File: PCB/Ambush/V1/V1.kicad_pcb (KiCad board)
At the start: 2 copper layers, 46.5 x 54.6 mm, 7 parts, among them J1 Pines Motores, J2 Screw_Terminal_01x02, SW1 SW ON/OFF, U2 ESP32-Devkit-V1

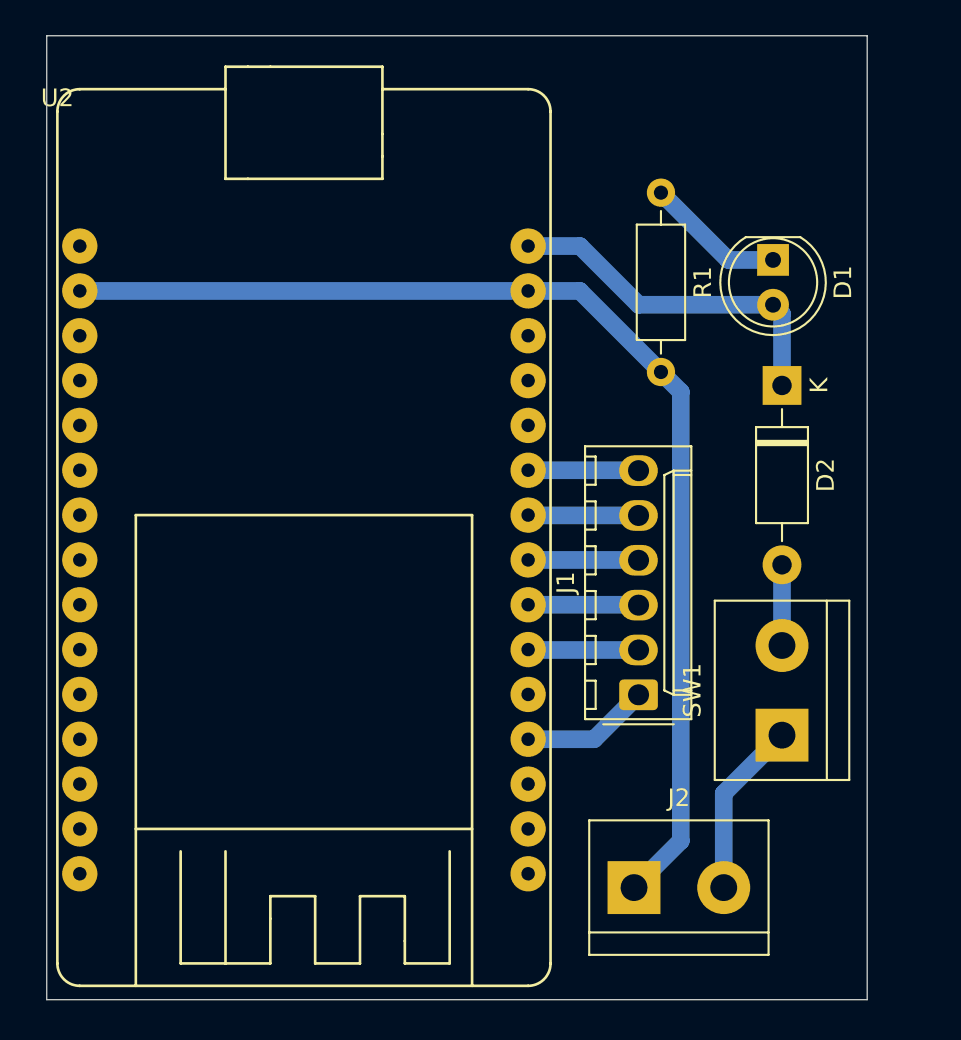
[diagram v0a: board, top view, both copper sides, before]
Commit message: PCB Con testpoint
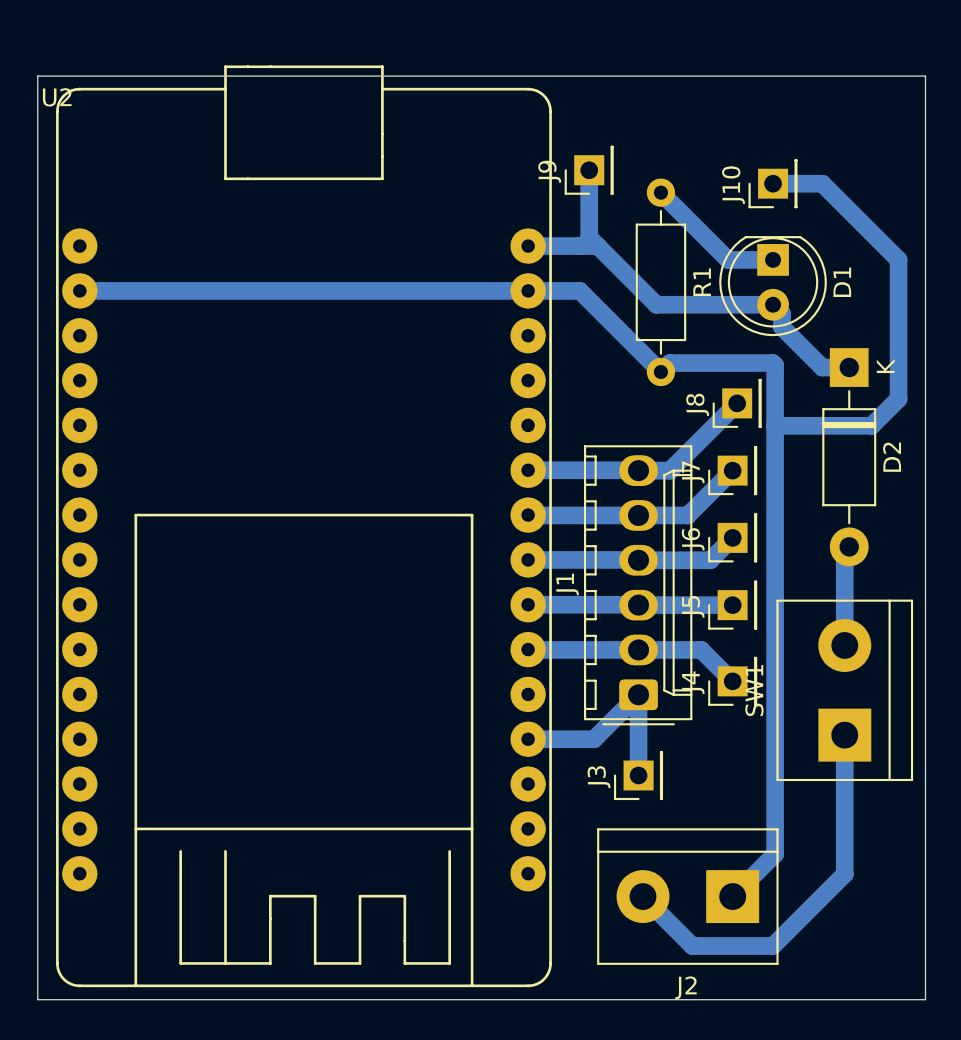
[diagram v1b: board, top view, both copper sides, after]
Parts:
- added J10: Conn_01x01_Pin, Connector_PinHeader_2.54mm:PinHeader_1x01_P2.54mm_Vertical, F.Cu at (141.2, 51.1)
- added J3: Conn_01x01_Pin, Connector_PinHeader_2.54mm:PinHeader_1x01_P2.54mm_Vertical, F.Cu at (133.6, 84.6)
- added J4: Conn_01x01_Pin, Connector_PinHeader_2.54mm:PinHeader_1x01_P2.54mm_Vertical, F.Cu at (138.9, 79.2)
- added J5: Conn_01x01_Pin, Connector_PinHeader_2.54mm:PinHeader_1x01_P2.54mm_Vertical, F.Cu at (138.9, 74.9)
- added J6: Conn_01x01_Pin, Connector_PinHeader_2.54mm:PinHeader_1x01_P2.54mm_Vertical, F.Cu at (138.9, 71.1)
- added J7: Conn_01x01_Pin, Connector_PinHeader_2.54mm:PinHeader_1x01_P2.54mm_Vertical, F.Cu at (138.9, 67.3)
- added J8: Conn_01x01_Pin, Connector_PinHeader_2.54mm:PinHeader_1x01_P2.54mm_Vertical, F.Cu at (139.2, 63.5)
- added J9: Conn_01x01_Pin, Connector_PinHeader_2.54mm:PinHeader_1x01_P2.54mm_Vertical, F.Cu at (130.8, 50.3)
- moved J2 5.61 mm to (138.9, 91.4), turned to 180 degrees
- moved D2 3.94 mm to (145.5, 61.5)
- moved SW1 3.56 mm to (145.3, 82.3)
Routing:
- net GND: track 65.6 -> 97.1 mm
- net Net-(J2-Pin_2): track 10.0 -> 22.1 mm
- net BIN 2 MONSTER SHIELD: track 6.26 -> 13.4 mm
- net AIN2 MONSTER SHIELD: track 6.26 -> 12.7 mm
- net PWM A MONSTER SHIELD: track 6.26 -> 12.3 mm
- net +5V: track 20.4 -> 26.3 mm
- net AIN1 MONSTER SHIELD: track 6.26 -> 12.1 mm
- net PWM B MONSTER SHIELD: track 6.26 -> 11.6 mm
- net BIN 1 MONSTER SHIELD: track 7.30 -> 11.9 mm
- net Net-(D2-A): track 4.57 -> 5.69 mm
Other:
- board size 46.5 x 54.6 mm -> 50.3 x 52.3 mm
